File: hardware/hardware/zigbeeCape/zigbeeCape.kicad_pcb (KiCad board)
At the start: 2 copper layers, 4 parts

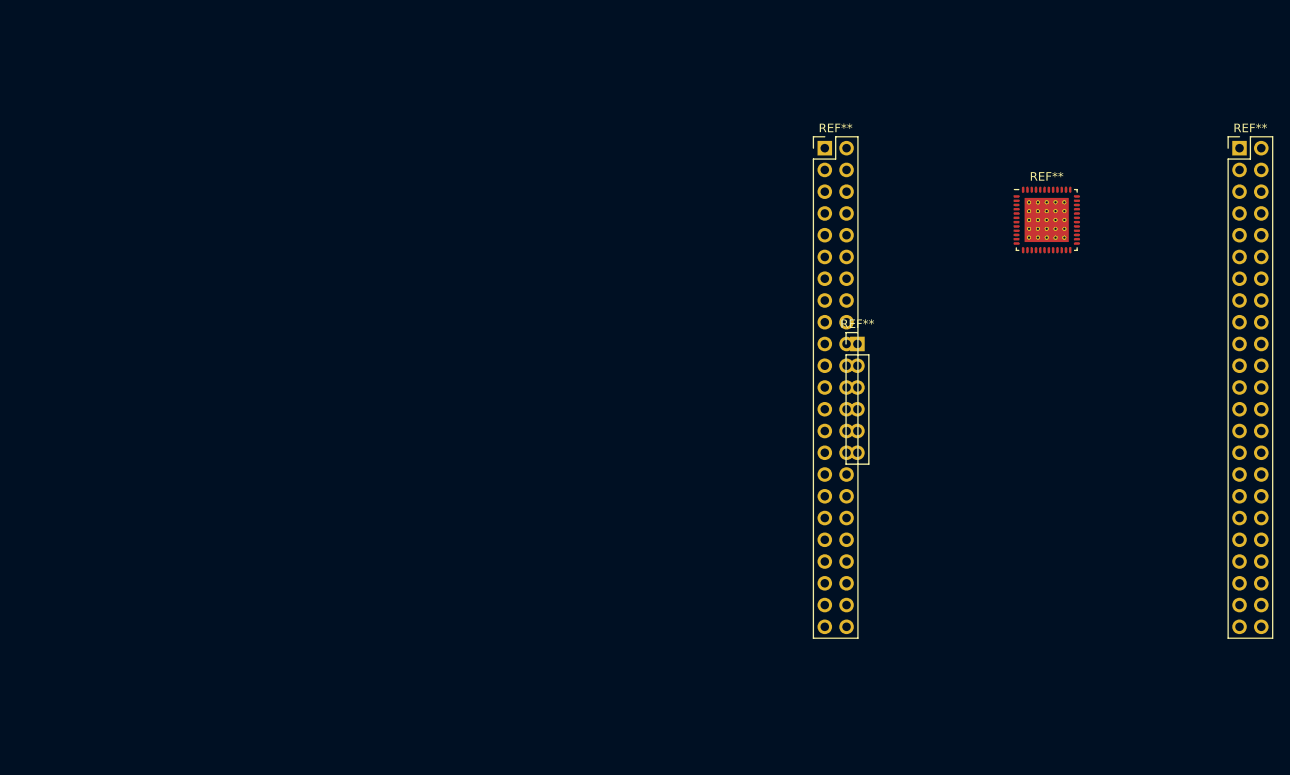
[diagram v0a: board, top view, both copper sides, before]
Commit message: Checked Schematic is correct. Added PCB outline and verified Pin spacing.
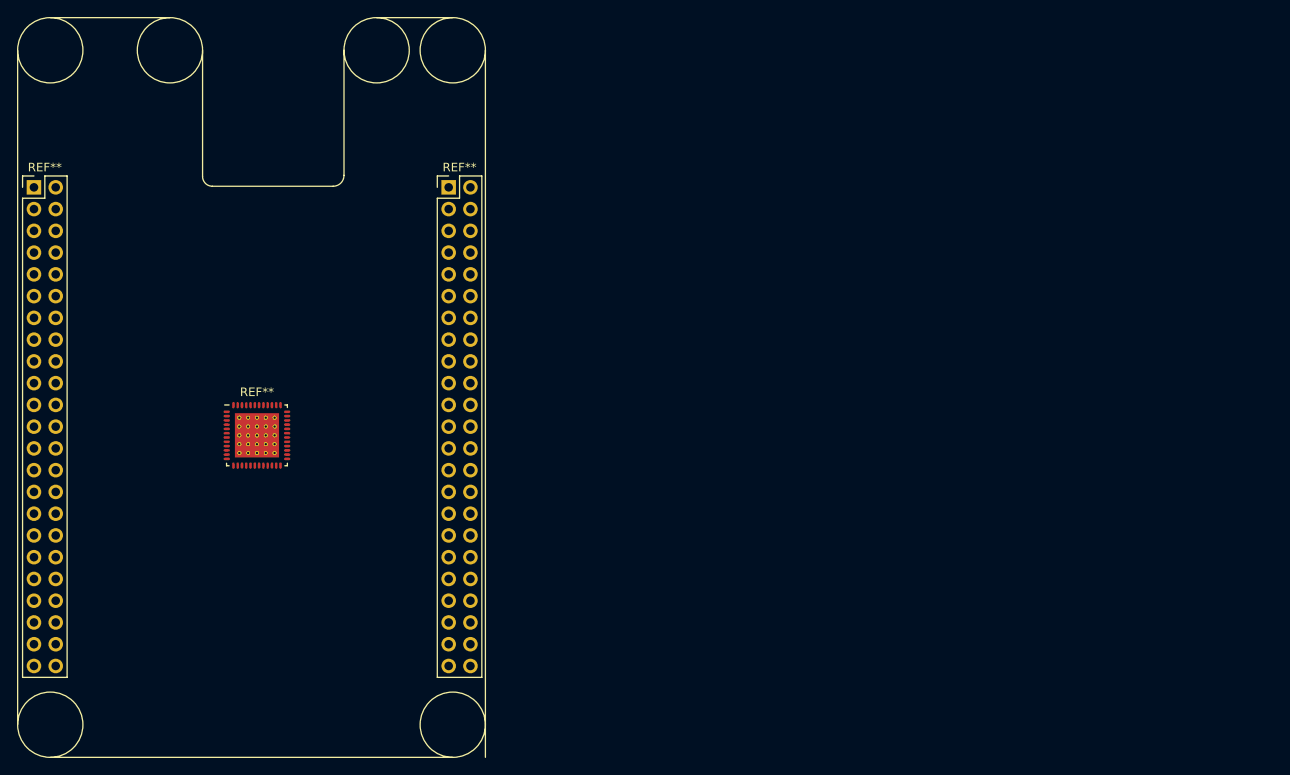
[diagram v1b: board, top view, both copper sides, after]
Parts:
- removed the REF** at (148.8, 88.9)
- removed the REF** at (145.0, 66.0)
- removed the REF** at (193.5, 66.0)
- added REF**: PinHeader_2x23_P2.54mm_Vertical, Connector_PinHeader_2.54mm:PinHeader_2x23_P2.54mm_Vertical, F.Cu at (52.7, 70.6)
- added REF**: PinHeader_2x23_P2.54mm_Vertical, Connector_PinHeader_2.54mm:PinHeader_2x23_P2.54mm_Vertical, F.Cu at (101.1, 70.6)
- moved REF** 95.6 mm to (78.7, 99.6)

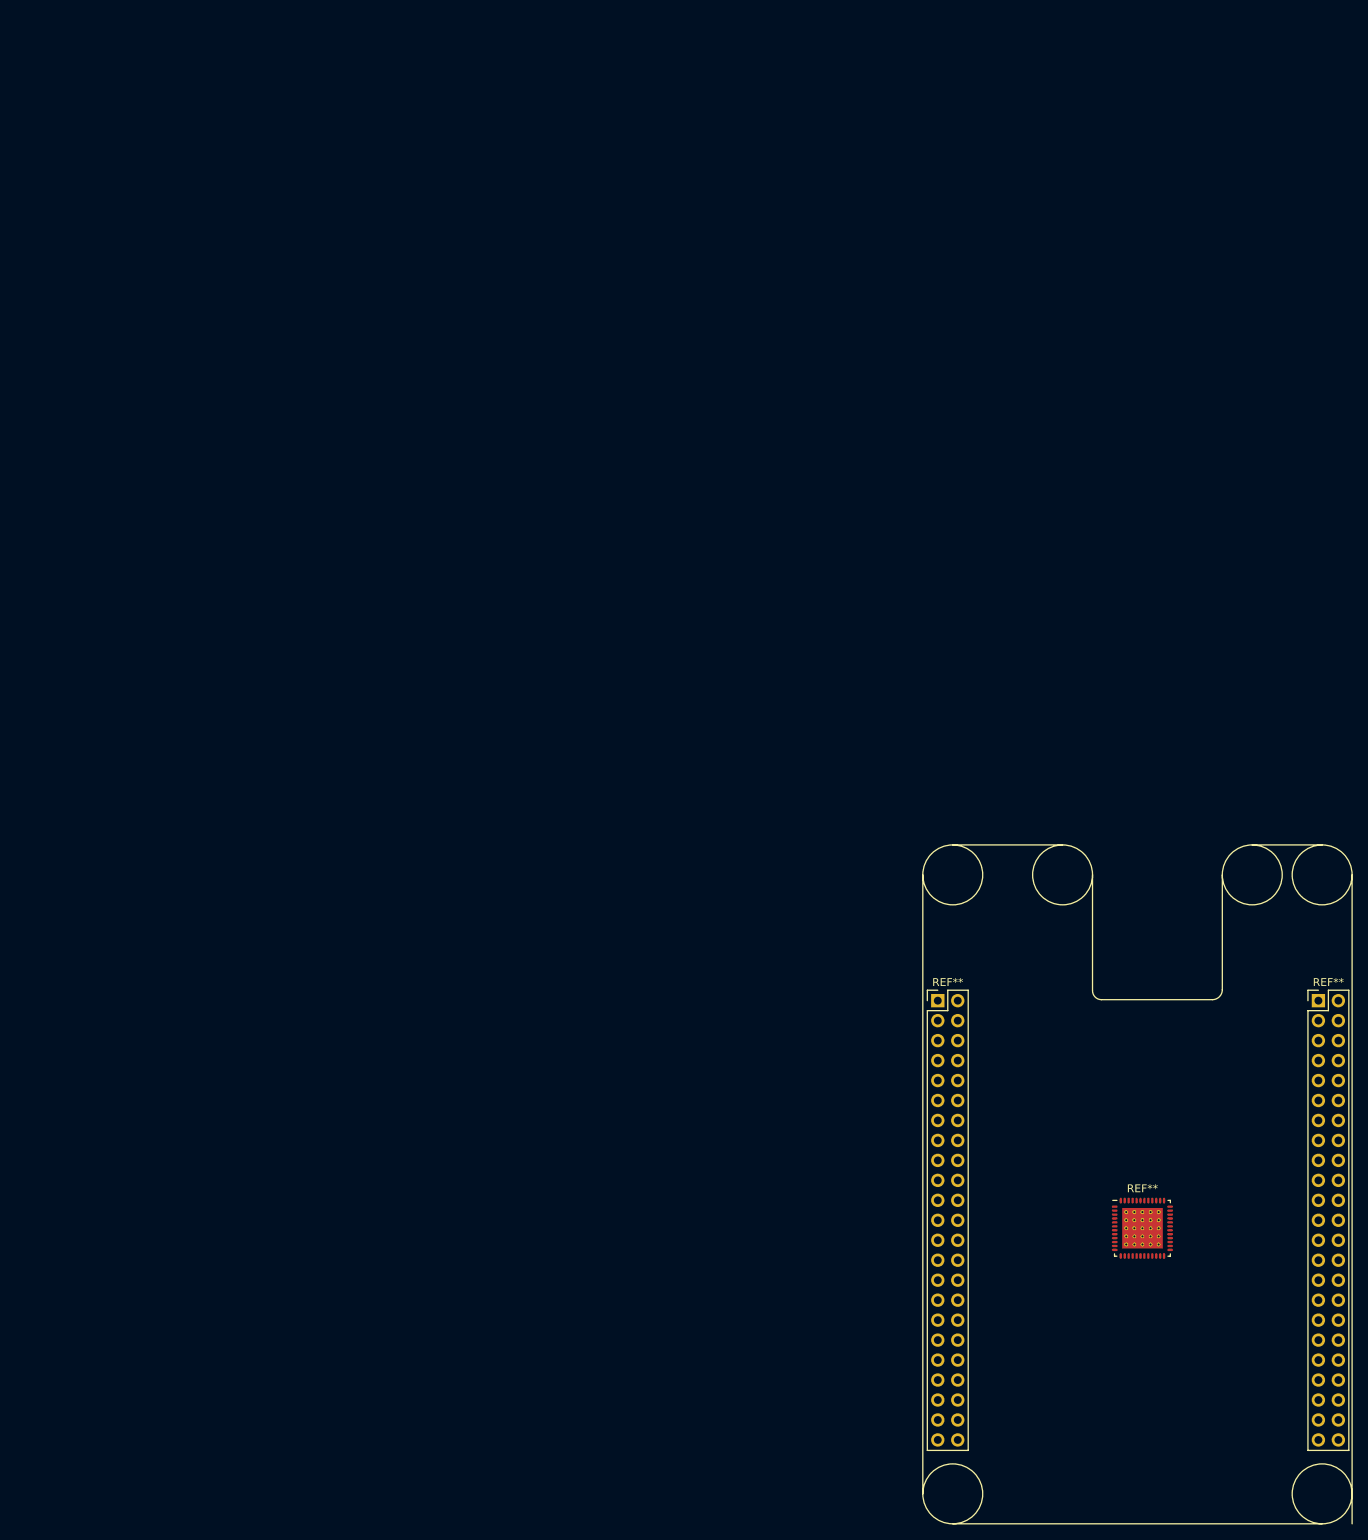
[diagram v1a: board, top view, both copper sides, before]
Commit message: Changed push button, Started layout
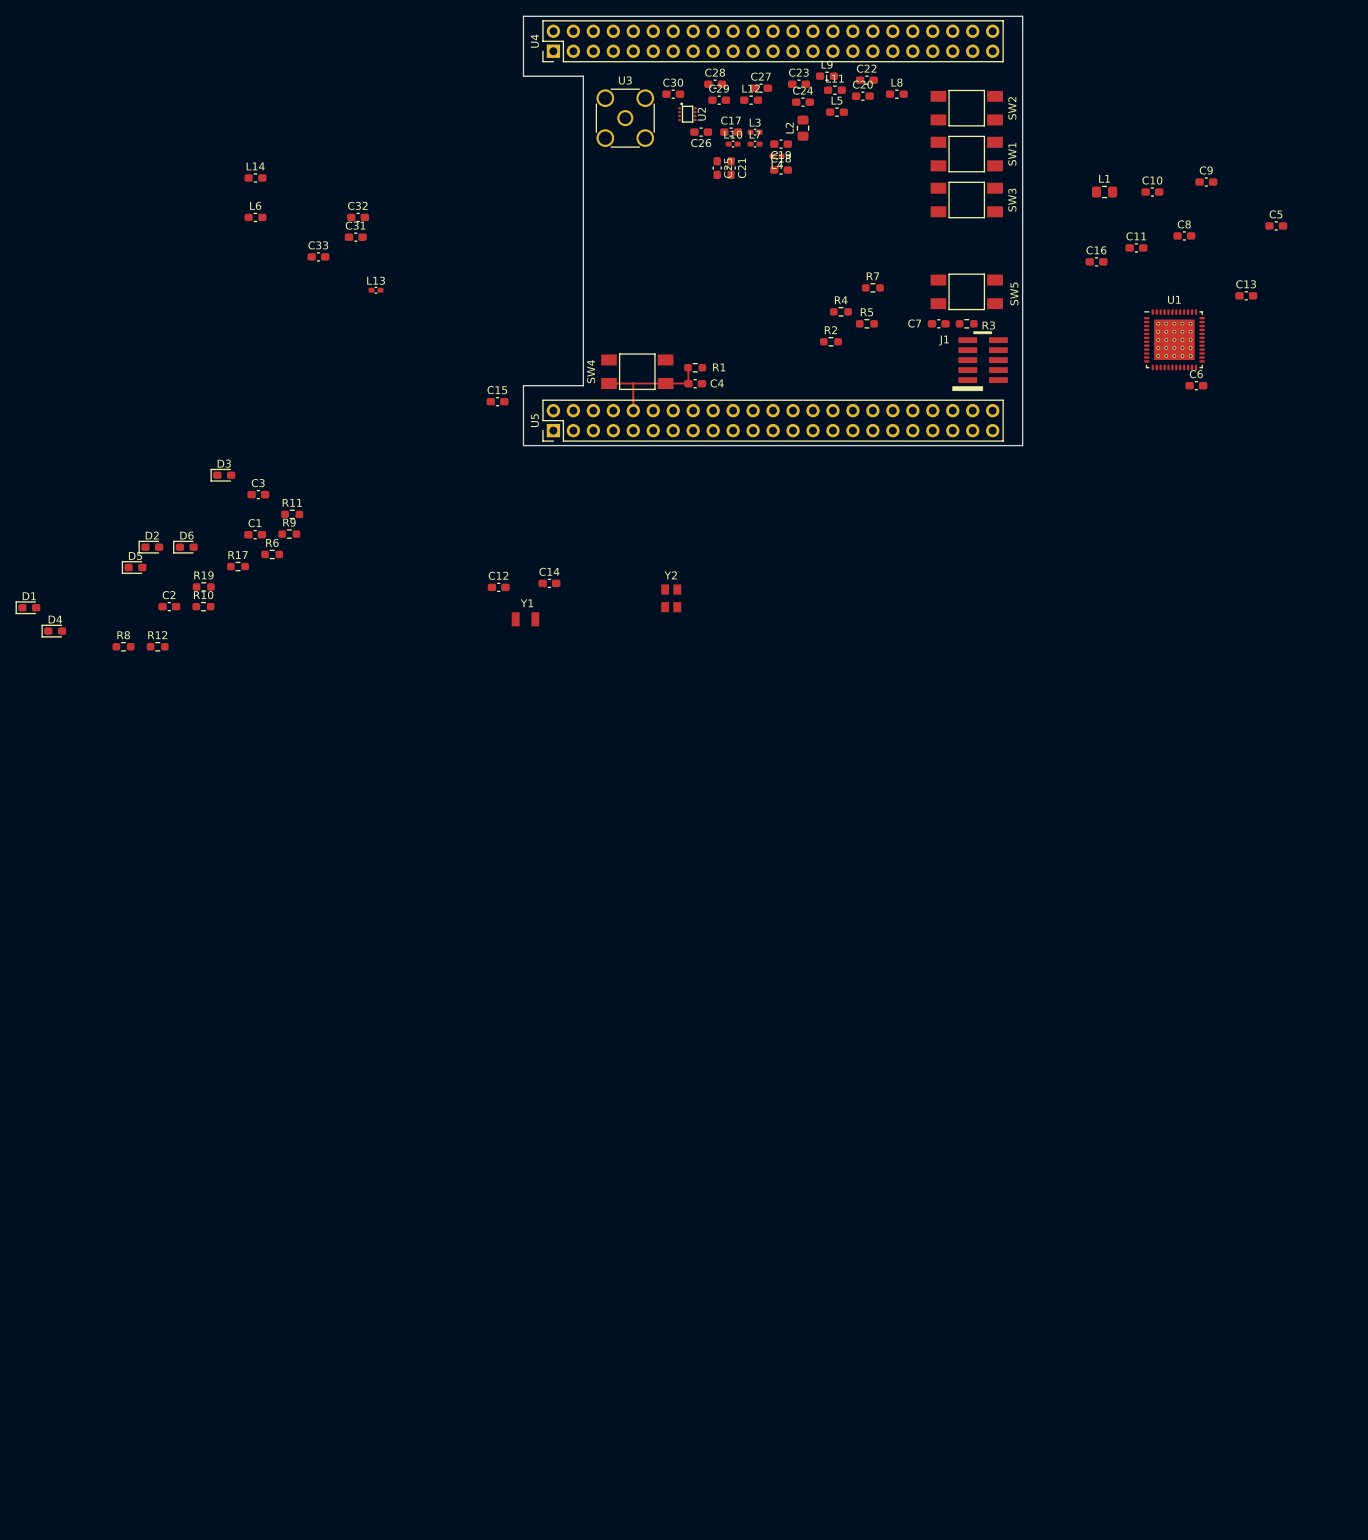
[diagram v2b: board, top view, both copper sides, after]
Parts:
- removed REF** (x2): PinHeader_2x23_P2.54mm_Vertical, Connector_PinHeader_2.54mm:PinHeader_2x23_P2.54mm_Vertical
- removed REF**: CC1352R, zigbeeCape:CC1352R
- added C1: DNM_1uF, Capacitor_SMD:C_0603_1608Metric_Pad1.08x0.95mm_HandSolder, F.Cu at (-34.1, 11.3)
- added C10: 22uF, Capacitor_SMD:C_0603_1608Metric_Pad1.08x0.95mm_HandSolder, F.Cu at (80.0, -32.3)
- added C11: 22uF, Capacitor_SMD:C_0603_1608Metric_Pad1.08x0.95mm_HandSolder, F.Cu at (78.0, -25.1)
- added C12: 12pF, Capacitor_SMD:C_0603_1608Metric_Pad1.08x0.95mm_HandSolder, F.Cu at (-3.15, 18.0)
- added C13: 0.1uF, Capacitor_SMD:C_0603_1608Metric_Pad1.08x0.95mm_HandSolder, F.Cu at (91.9, -19.1)
- added C14: 12pF, Capacitor_SMD:C_0603_1608Metric_Pad1.08x0.95mm_HandSolder, F.Cu at (3.30, 17.5)
- added C15: 1uF, Capacitor_SMD:C_0603_1608Metric_Pad1.08x0.95mm_HandSolder, F.Cu at (-3.30, -5.59)
- added C16: 0.1uF, Capacitor_SMD:C_0603_1608Metric_Pad1.08x0.95mm_HandSolder, F.Cu at (72.9, -23.4)
- added C17: 12pF, Capacitor_SMD:C_0603_1608Metric_Pad1.08x0.95mm_HandSolder, F.Cu at (26.4, -39.9)
- added C18: 1.1pF, Capacitor_SMD:C_0603_1608Metric_Pad1.08x0.95mm_HandSolder, F.Cu at (32.8, -35.1)
- added C19: 1.1pF, Capacitor_SMD:C_0603_1608Metric_Pad1.08x0.95mm_HandSolder, F.Cu at (32.8, -38.4)
- added C2: DNM_1uF, Capacitor_SMD:C_0603_1608Metric_Pad1.08x0.95mm_HandSolder, F.Cu at (-45.1, 20.5)
- added C20: 1.2pF, Capacitor_SMD:C_0603_1608Metric_Pad1.08x0.95mm_HandSolder, F.Cu at (43.2, -44.5)
- added C21: 1pF, Capacitor_SMD:C_0603_1608Metric_Pad1.08x0.95mm_HandSolder, F.Cu at (26.4, -35.3)
- added C22: 100pF, Capacitor_SMD:C_0603_1608Metric_Pad1.08x0.95mm_HandSolder, F.Cu at (43.7, -46.5)
- added C23: 3pF, Capacitor_SMD:C_0603_1608Metric_Pad1.08x0.95mm_HandSolder, F.Cu at (35.1, -46.0)
- added C24: 3pF, Capacitor_SMD:C_0603_1608Metric_Pad1.08x0.95mm_HandSolder, F.Cu at (35.6, -43.7)
- added C25: DNM, Capacitor_SMD:C_0603_1608Metric_Pad1.08x0.95mm_HandSolder, F.Cu at (24.6, -35.3)
- added C26: 12pF, Capacitor_SMD:C_0603_1608Metric_Pad1.08x0.95mm_HandSolder, F.Cu at (22.6, -39.9)
- added C27: DNM, Capacitor_SMD:C_0603_1608Metric_Pad1.08x0.95mm_HandSolder, F.Cu at (30.2, -45.5)
- added C28: 3.6pF, Capacitor_SMD:C_0603_1608Metric_Pad1.08x0.95mm_HandSolder, F.Cu at (24.4, -46.0)
- added C29: 100pF, Capacitor_SMD:C_0603_1608Metric_Pad1.08x0.95mm_HandSolder, F.Cu at (24.9, -43.9)
- added C3: DNM_1uF, Capacitor_SMD:C_0603_1608Metric_Pad1.08x0.95mm_HandSolder, F.Cu at (-33.7, 6.24)
- added C30: DNM, Capacitor_SMD:C_0603_1608Metric_Pad1.08x0.95mm_HandSolder, F.Cu at (19.1, -44.7)
- added C31: 100pF, Capacitor_SMD:C_0603_1608Metric_Pad1.08x0.95mm_HandSolder, F.Cu at (-21.3, -26.5)
- added C32: DNM, Capacitor_SMD:C_0603_1608Metric_Pad1.08x0.95mm_HandSolder, F.Cu at (-21.0, -29.0)
- added C33: 5.6pF, Capacitor_SMD:C_0603_1608Metric_Pad1.08x0.95mm_HandSolder, F.Cu at (-26.1, -24.0)
- added C4: DNM_2.2uF, Capacitor_SMD:C_0603_1608Metric_Pad1.08x0.95mm_HandSolder, F.Cu at (21.8, -7.87)
- added C5: 0.1uF, Capacitor_SMD:C_0603_1608Metric_Pad1.08x0.95mm_HandSolder, F.Cu at (95.8, -27.9)
- added C6: 0.1uF, Capacitor_SMD:C_0603_1608Metric_Pad1.08x0.95mm_HandSolder, F.Cu at (85.6, -7.62)
- added C7: 2.2uF, Capacitor_SMD:C_0603_1608Metric_Pad1.08x0.95mm_HandSolder, F.Cu at (52.8, -15.5)
- added C8: 0.1uF, Capacitor_SMD:C_0603_1608Metric_Pad1.08x0.95mm_HandSolder, F.Cu at (84.1, -26.7)
- added C9: 0.1uF, Capacitor_SMD:C_0603_1608Metric_Pad1.08x0.95mm_HandSolder, F.Cu at (86.9, -33.5)
- added D1: Blue, LED_SMD:LED_0603_1608Metric_Pad1.05x0.95mm_HandSolder, F.Cu at (-62.9, 20.6)
- added D2: Blue, LED_SMD:LED_0603_1608Metric_Pad1.05x0.95mm_HandSolder, F.Cu at (-47.2, 12.9)
- added D3: Blue, LED_SMD:LED_0603_1608Metric_Pad1.05x0.95mm_HandSolder, F.Cu at (-38.1, 3.77)
- added D4: Blue, LED_SMD:LED_0603_1608Metric_Pad1.05x0.95mm_HandSolder, F.Cu at (-59.6, 23.6)
- added D5: Blue, LED_SMD:LED_0603_1608Metric_Pad1.05x0.95mm_HandSolder, F.Cu at (-49.4, 15.5)
- added D6: Green, LED_SMD:LED_0603_1608Metric_Pad1.05x0.95mm_HandSolder, F.Cu at (-42.8, 12.9)
- added J1: Conn_ARM_JTAG_SWD_10, zigbeeCape:Conn_ARM_JTAG_SWD_10, F.Cu at (58.4, -10.4)
- added L1: 6.8uH, Inductor_SMD:L_0805_2012Metric_Pad1.15x1.40mm_HandSolder, F.Cu at (73.9, -32.3)
- added L10: 2nH, Inductor_SMD:L_0402_1005Metric_Pad0.77x0.64mm_HandSolder, F.Cu at (26.7, -38.4)
- added L11: 10nH, Inductor_SMD:L_0603_1608Metric_Pad1.05x0.95mm_HandSolder, F.Cu at (39.6, -45.2)
- added L12: 9.1nH, Inductor_SMD:L_0603_1608Metric_Pad1.05x0.95mm_HandSolder, F.Cu at (29.0, -43.9)
- added L13: 3.3nH, Inductor_SMD:L_0402_1005Metric_Pad0.77x0.64mm_HandSolder, F.Cu at (-18.8, -19.8)
- added L14: DNM, Inductor_SMD:L_0603_1608Metric_Pad1.05x0.95mm_HandSolder, F.Cu at (-34.1, -34.0)
- added L2: 15nH, Inductor_SMD:L_0805_2012Metric_Pad1.15x1.40mm_HandSolder, F.Cu at (35.6, -40.4)
- added L3: 2.4nH, Inductor_SMD:L_0402_1005Metric_Pad0.77x0.64mm_HandSolder, F.Cu at (29.5, -39.9)
- added L4: 2.4nH, Inductor_SMD:L_0402_1005Metric_Pad0.77x0.64mm_HandSolder, F.Cu at (32.3, -36.8)
- added L5: 3.9nH, Inductor_SMD:L_0603_1608Metric_Pad1.05x0.95mm_HandSolder, F.Cu at (39.9, -42.4)
- added L6: 3.9nH, Inductor_SMD:L_0603_1608Metric_Pad1.05x0.95mm_HandSolder, F.Cu at (-34.1, -29.0)
- added L7: 2nH, Inductor_SMD:L_0402_1005Metric_Pad0.77x0.64mm_HandSolder, F.Cu at (29.5, -38.4)
- added L8: 22nH, Inductor_SMD:L_0603_1608Metric_Pad1.05x0.95mm_HandSolder, F.Cu at (47.5, -44.7)
- added L9: 10nH, Inductor_SMD:L_0603_1608Metric_Pad1.05x0.95mm_HandSolder, F.Cu at (38.6, -47.0)
- added R1: DNM_10k, Resistor_SMD:R_0603_1608Metric_Pad0.98x0.95mm_HandSolder, F.Cu at (21.8, -9.91)
- added R10: 1k, Resistor_SMD:R_0603_1608Metric_Pad0.98x0.95mm_HandSolder, F.Cu at (-40.7, 20.5)
- added R11: 1k, Resistor_SMD:R_0603_1608Metric_Pad0.98x0.95mm_HandSolder, F.Cu at (-29.4, 8.75)
- added R12: 1k, Resistor_SMD:R_0603_1608Metric_Pad0.98x0.95mm_HandSolder, F.Cu at (-46.5, 25.6)
- added R17: 4.7k, Resistor_SMD:R_0603_1608Metric_Pad0.98x0.95mm_HandSolder, F.Cu at (-36.3, 15.4)
- added R19: 4.7k, Resistor_SMD:R_0603_1608Metric_Pad0.98x0.95mm_HandSolder, F.Cu at (-40.7, 18.0)
- added R2: 10K, Resistor_SMD:R_0603_1608Metric_Pad0.98x0.95mm_HandSolder, F.Cu at (39.1, -13.2)
- added R3: DNM_10K, Resistor_SMD:R_0603_1608Metric_Pad0.98x0.95mm_HandSolder, F.Cu at (56.4, -15.5)
- added R4: 10K, Resistor_SMD:R_0603_1608Metric_Pad0.98x0.95mm_HandSolder, F.Cu at (40.4, -17.0)
- added R5: 10K, Resistor_SMD:R_0603_1608Metric_Pad0.98x0.95mm_HandSolder, F.Cu at (43.7, -15.5)
- added R6: 1k, Resistor_SMD:R_0603_1608Metric_Pad0.98x0.95mm_HandSolder, F.Cu at (-32.0, 13.8)
- added R7: 10K, Resistor_SMD:R_0603_1608Metric_Pad0.98x0.95mm_HandSolder, F.Cu at (44.5, -20.1)
- added R8: 1k, Resistor_SMD:R_0603_1608Metric_Pad0.98x0.95mm_HandSolder, F.Cu at (-50.9, 25.6)
- added R9: 1k, Resistor_SMD:R_0603_1608Metric_Pad0.98x0.95mm_HandSolder, F.Cu at (-29.8, 11.3)
- added SW1: SW_MEC_5E, zigbeeCape:SMD_PUSH_BUTTON, F.Cu at (56.4, -37.1)
- added SW2: SW_MEC_5E, zigbeeCape:SMD_PUSH_BUTTON, F.Cu at (56.4, -42.9)
- added SW3: SW_MEC_5E, zigbeeCape:SMD_PUSH_BUTTON, F.Cu at (56.4, -31.2)
- added SW4: SW_MEC_5E, zigbeeCape:SMD_PUSH_BUTTON, F.Cu at (14.5, -9.40)
- added SW5: SW_MEC_5E, zigbeeCape:SMD_PUSH_BUTTON, F.Cu at (56.4, -19.6)
- added U1: CC1352R, zigbeeCape:CC1352R, F.Cu at (82.8, -13.5)
- added U2: 0.8Ghz_and_2.4GHz_Filter, zigbeeCape:DPX252690DT-5032B1, F.Cu at (20.8, -42.2)
- added U3: SMA_Antenna, Connector_Coaxial:SMA_Amphenol_132134-16_Vertical, F.Cu at (13.0, -41.7)
- added U4: BeagleBone_P8, Connector_PinHeader_2.54mm:PinHeader_2x23_P2.54mm_Vertical, F.Cu at (31.8, -51.4)
- added U5: BeagleBone_P9, Connector_PinHeader_2.54mm:PinHeader_2x23_P2.54mm_Vertical, F.Cu at (31.8, -3.17)
- added Y1: 32.768kHz, zigbeeCape:FC-135_Crystal_Unit, F.Cu at (0.51, 22.1)
- added Y2: 48MHz, zigbeeCape:SXT32418FD16-48MHZ_Crystal, F.Cu at (18.8, 19.6)
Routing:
- net /BeagleBone_Headers/BeagleBone_Reset: track 0.00 -> 15.6 mm
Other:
- board outline added: 63.5 x 54.6 mm
- copper layers 2 -> 4
- net class Default: clearance 0.2 -> 0.254; trace_width 0.25 -> 0.254
- rule trace_clearance: 0.2 -> 0.254

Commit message: Layout Planning done, uC Done
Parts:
- moved C12 87.9 mm to (40.5, -58.3)
- moved C14 85.9 mm to (37.0, -61.5)
- moved Y1 85.6 mm to (28.5, -58.8)
- moved L6 69.7 mm to (35.6, -31.2), turned to 180 degrees
- moved Y2 66.9 mm to (37.3, -44.7)
- moved C5 57.8 mm to (40.6, -45.2), turned to 90 degrees
- moved C15 55.6 mm to (46.0, -31.2), turned to 270 degrees
- moved C13 52.9 mm to (46.2, -45.6), turned to 90 degrees
- moved C6 52.1 mm to (39.1, -31.2), turned to 270 degrees
- moved U1 46.7 mm to (42.7, -37.3)
- moved C8 40.1 mm to (44.2, -31.2), turned to 270 degrees
- moved C11 39.2 mm to (44.6, -45.6), turned to 90 degrees
- moved C9 38.3 mm to (48.8, -37.6)
- moved C16 37.3 mm to (42.9, -45.6), turned to 90 degrees
- moved SW3 32.7 mm to (87.6, -40.9)
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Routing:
- net GND: track 0.00 -> 58.8 mm, vias 0 -> 32
- net Net-(C7-Pad1): track 0.00 -> 28.7 mm
- net Net-(J1-Pad8): track 0.00 -> 19.1 mm
- net Net-(J1-Pad6): track 0.00 -> 17.8 mm
- net Net-(J1-Pad4): track 0.00 -> 16.7 mm
- net Net-(J1-Pad2): track 0.00 -> 16.7 mm
- net +3V3: track 0.00 -> 13.8 mm, vias 0 -> 7
- net VDDR: track 0.00 -> 13.8 mm, vias 0 -> 2
- net Net-(C20-Pad2): track 0.00 -> 11.3 mm, vias 0 -> 2
- net /ZigBeeFiltering/2_4_GHZ_RF_P: track 0.00 -> 11.1 mm, vias 0 -> 2
- net Net-(U1-Pad47): track 0.00 -> 10.2 mm
- net Net-(C20-Pad1): track 0.00 -> 7.75 mm
- net /ZigBeeFiltering/2_4_GHZ_RF_N: track 0.00 -> 7.61 mm
- net DCDC_SW: track 0.00 -> 6.51 mm, vias 0 -> 2
- net Net-(C30-Pad1): track 0.00 -> 5.69 mm
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- added copper zone on +3.3V, net +3V3
- added copper zone on Ground, net GND
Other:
- rule trace_min: 0.2 -> 0.1524
